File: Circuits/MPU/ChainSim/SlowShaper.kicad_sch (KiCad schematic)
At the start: 34 parts, among them U5 ADA4805-2ARMZ, U6 ADA4805-2ARMZ

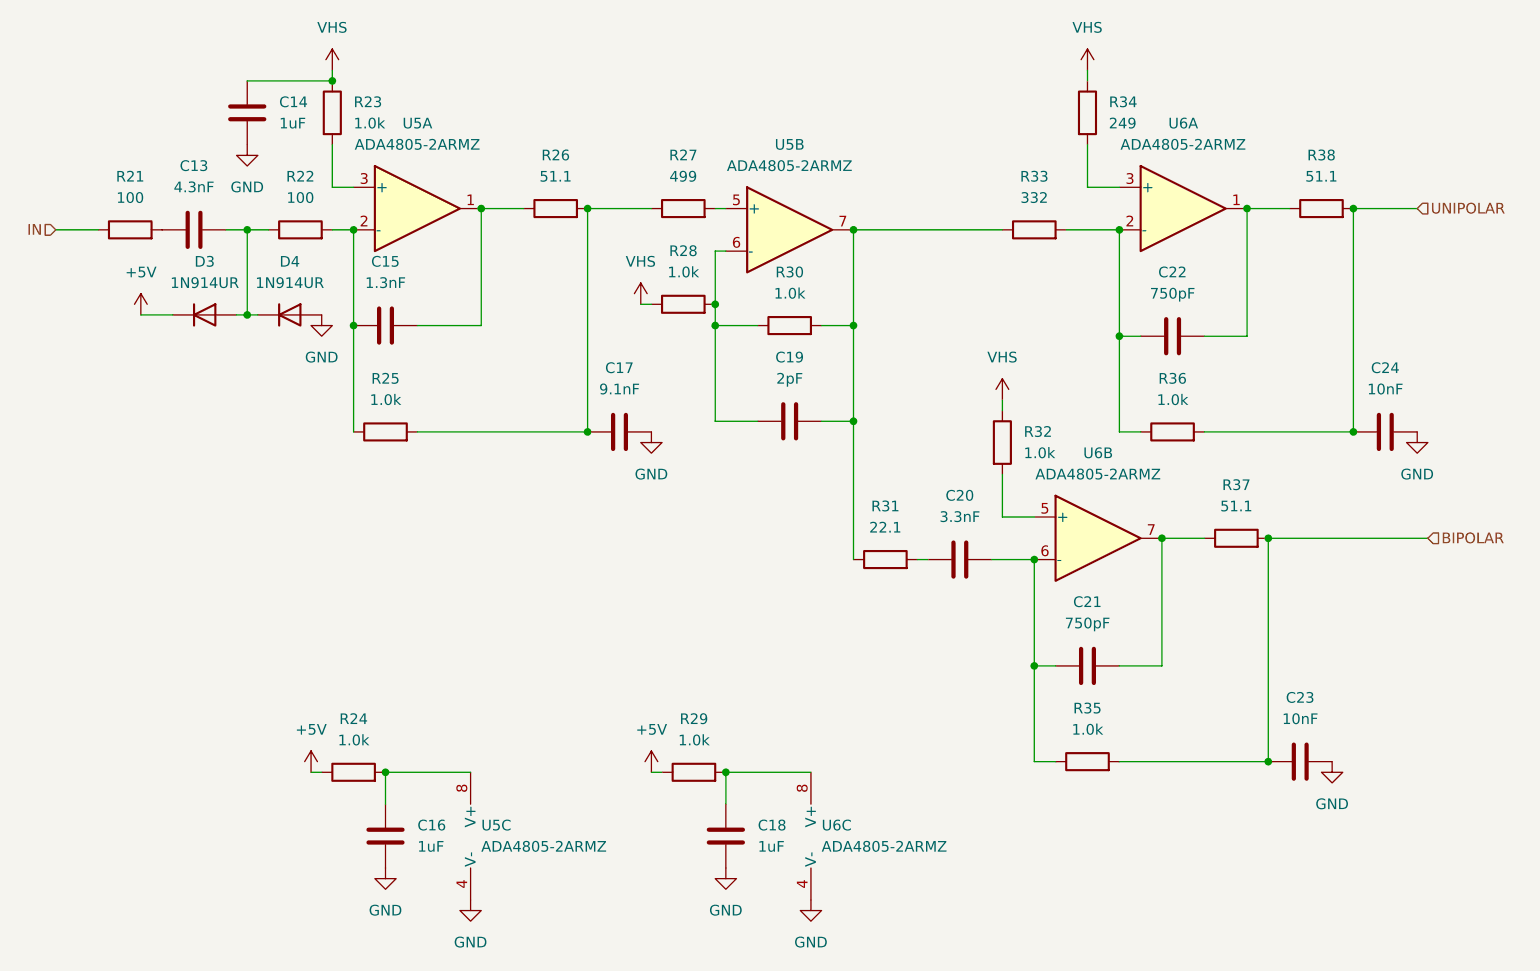
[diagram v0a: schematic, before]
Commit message: Chainsim working, a little tuneup
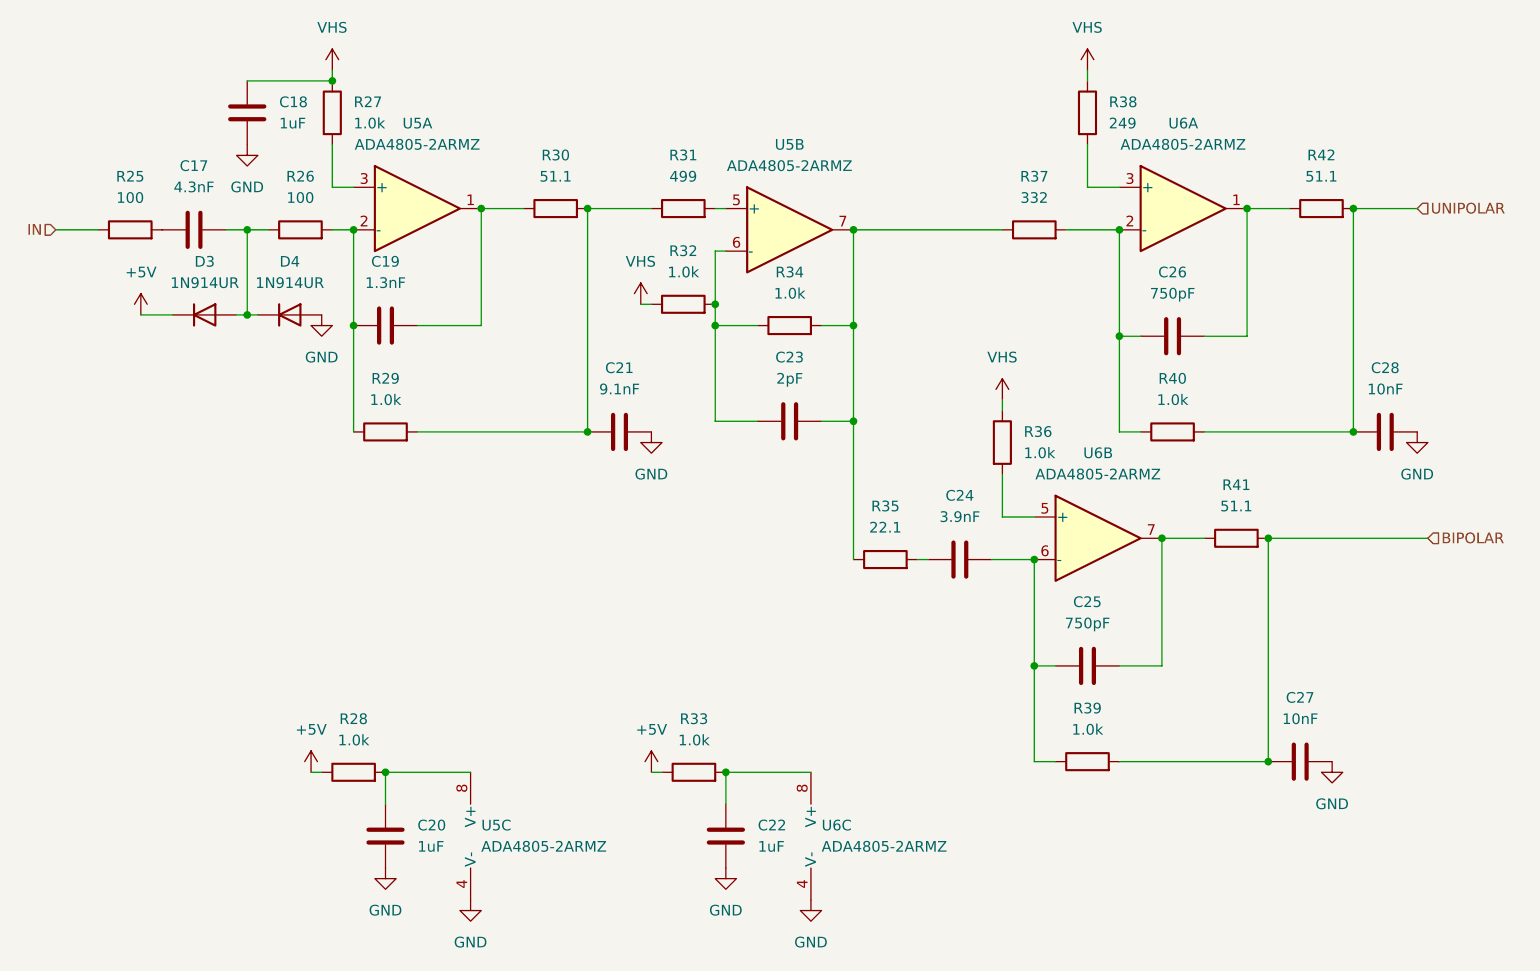
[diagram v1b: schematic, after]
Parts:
- C24: renamed from C20; value 3.3nF -> 3.9nF
- renumbered C13 to C17, C14 to C18, C15 to C19, C16 to C20, C17 to C21, C18 to C22, C19 to C23, C21 to C25, C22 to C26, C23 to C27, C24 to C28, R21 to R25, R22 to R26, R23 to R27, R24 to R28, R25 to R29, R26 to R30, R27 to R31, R28 to R32, R29 to R33, R30 to R34, R31 to R35, R32 to R36, R33 to R37, R34 to R38, R35 to R39, R36 to R40, R37 to R41, R38 to R42
